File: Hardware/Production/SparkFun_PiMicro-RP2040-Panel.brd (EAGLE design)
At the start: 132.1 x 140.2 mm, 1551 parts, among them J1 Qwiic, J12 USB Female Type C Connector, J13 Qwiic, J16 USB Female Type C Connector, J17 Qwiic, J2 Qwiic, J20 USB Female Type C Connector, J21 Qwiic, J24 USB Female Type C Connector, J25 Qwiic, J28 USB Female Type C Connector, J29 Qwiic, J32 USB Female Type C Connector, J33 Qwiic, J36 USB Female Type C Connector, J37 Qwiic, J40 USB Female Type C Connector, J41 Qwiic, J44 USB Female Type C Connector, J45 Qwiic, J48 USB Female Type C Connector, J49 Qwiic, J5 USB Female Type C Connector, J52 USB Female Type C Connector, J53 Qwiic, J56 USB Female Type C Connector, J57 Qwiic, J60 USB Female Type C Connector, J8 USB Female Type C Connector, J9 Qwiic, U1 3.3V, U10 RP2040, U11 W25QXX128MBIT, U12 WS2812-2020, U13 3.3V, U14 RP2040, U15 W25QXX128MBIT, U16 WS2812-2020, U17 3.3V, U18 RP2040, U19 W25QXX128MBIT, U2 RP2040, U20 WS2812-2020, U21 3.3V, U22 RP2040, U23 W25QXX128MBIT, U24 WS2812-2020, U25 3.3V, U26 RP2040, U27 W25QXX128MBIT, U28 WS2812-2020, U29 3.3V, U3 WS2812-2020, U30 RP2040, U31 W25QXX128MBIT, U32 WS2812-2020, U33 3.3V, U34 RP2040, U35 W25QXX128MBIT, U36 WS2812-2020, U37 3.3V, U38 RP2040, U39 W25QXX128MBIT, U4 W25QXX128MBIT, U40 WS2812-2020, U41 3.3V, U42 RP2040, U43 W25QXX128MBIT, U44 WS2812-2020, U45 3.3V, U46 RP2040, U47 W25QXX128MBIT, U48 WS2812-2020, U49 3.3V, U5 3.3V, U50 RP2040, U51 W25QXX128MBIT, U52 WS2812-2020, U53 3.3V, U54 RP2040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

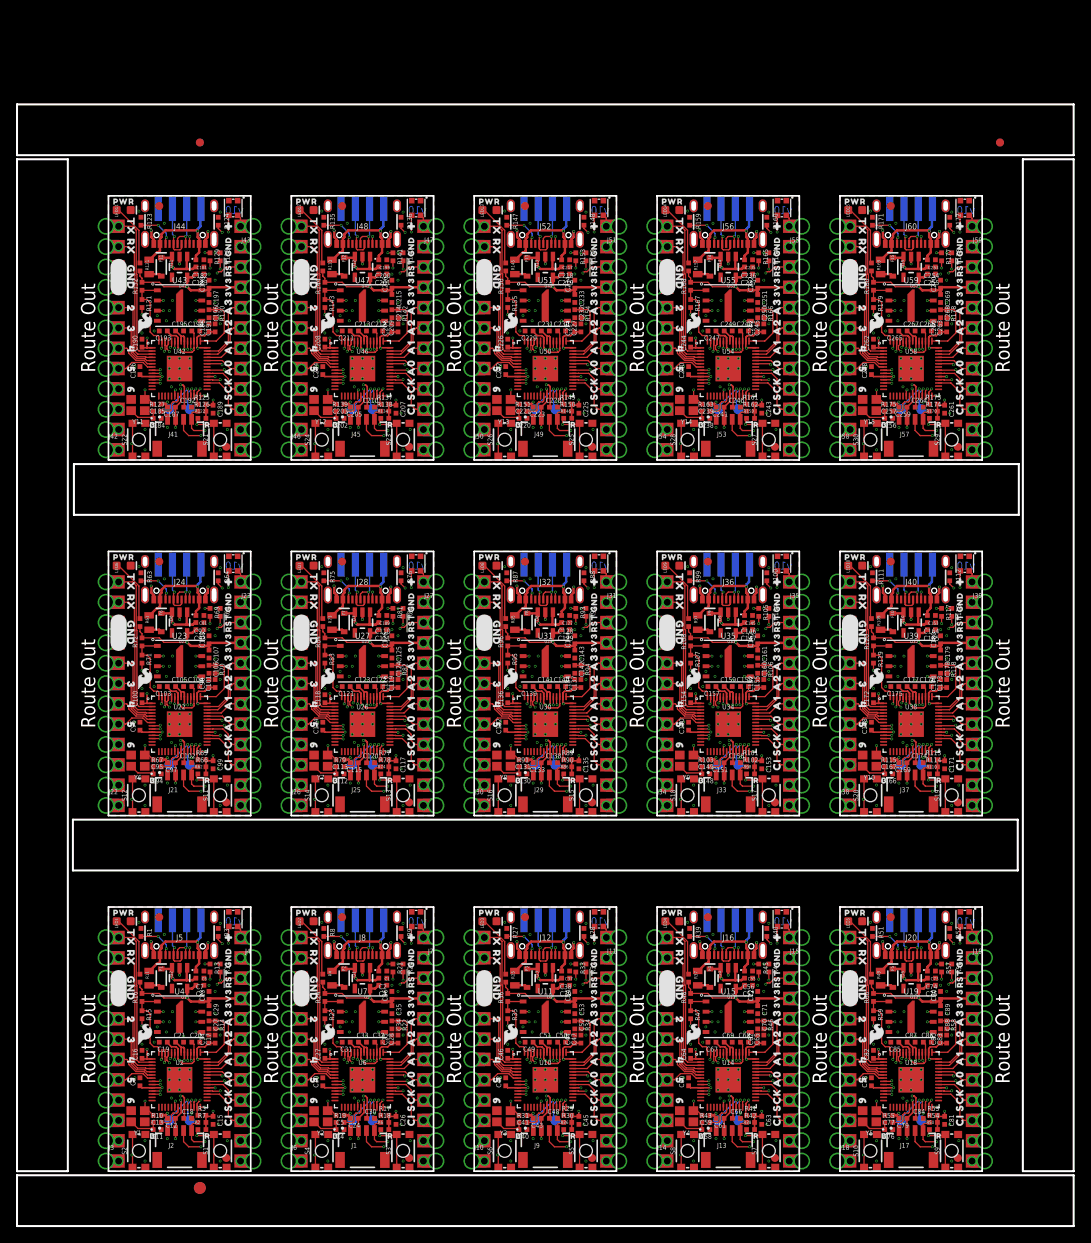
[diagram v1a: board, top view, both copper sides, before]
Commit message: Add DO TP for WS2812
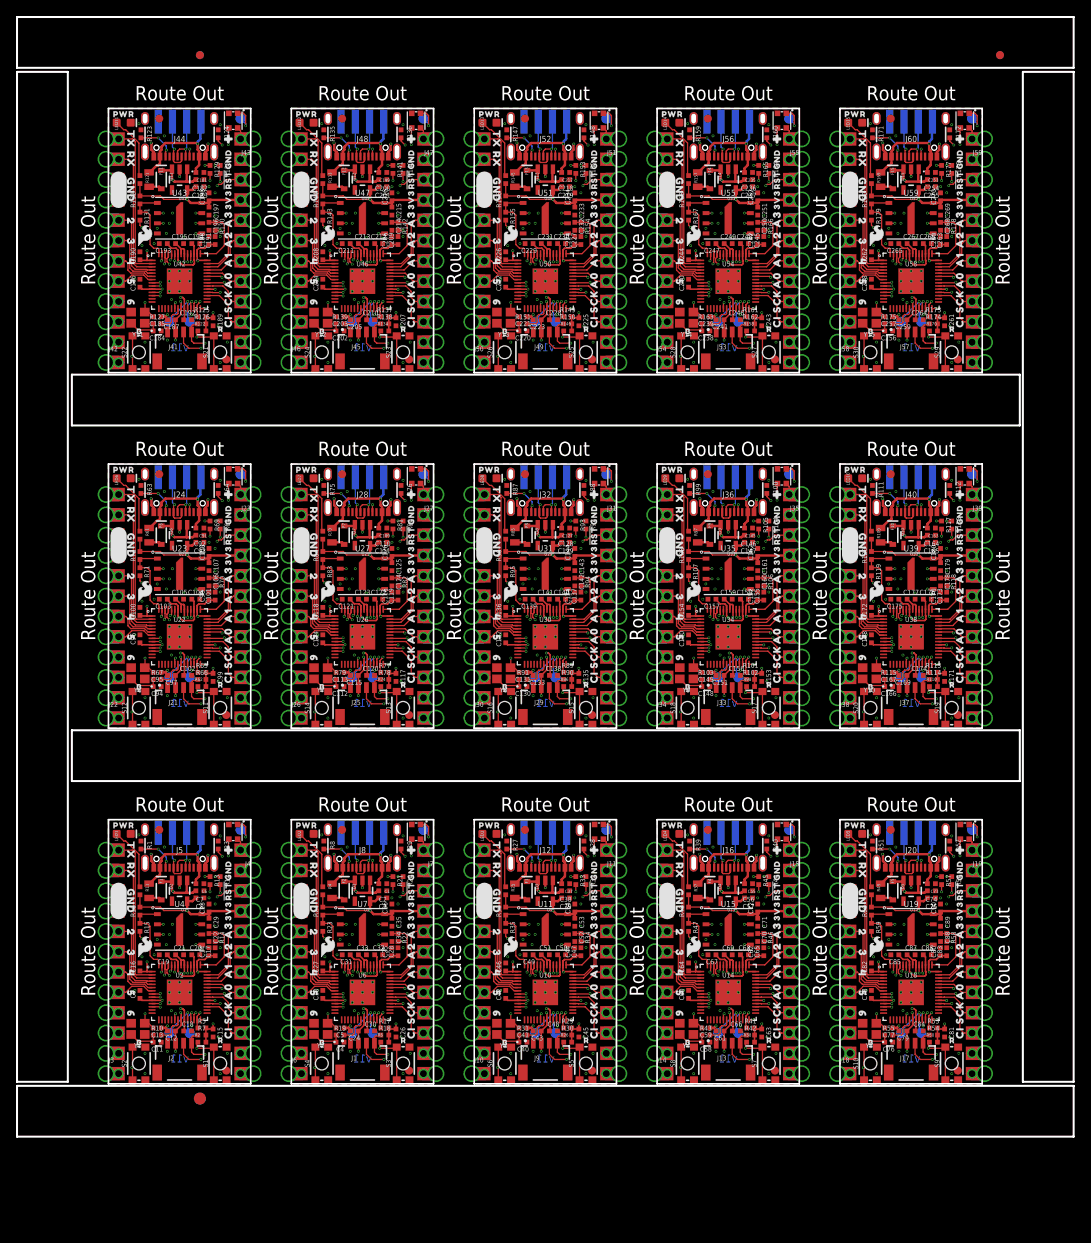
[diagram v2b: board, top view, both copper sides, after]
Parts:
- added TP31, TP32, TP33, TP34, TP35, TP36, TP37, TP38, TP39, TP40, TP41, TP42, TP43, TP44, TP45: (no value), SparkFun-Connectors:PAD.03X.05
- added U$766, U$790: (no value), output:31
- added U$767, U$791: (no value), output:42
- added U$768, U$792: (no value), output:53
- added U$769, U$793: (no value), output:64
- added U$770: (no value), output:#RST#1
- added U$771: (no value), output:3V30
- added U$772: (no value), output:PWR0
- added U$773, U$788, U$801: (no value), output:GND2
- added U$774, U$787: (no value), output:RX1
- added U$775, U$786: (no value), output:TX0
- added U$776: (no value), output:GND_0
- added U$777: (no value), output:70
- added U$778: (no value), output:81
- added U$779: (no value), output:92
- added U$780: (no value), output:CI4
- added U$781: (no value), output:SCK3
- added U$782: (no value), output:A00
- added U$783: (no value), output:A10
- added U$784: (no value), output:A21
- added U$785: (no value), output:A32
- added U$789: (no value), output:20
- added U$794: (no value), output:D#1
- added U$795: (no value), output:D#2
- added U$796: (no value), output:G0
- added U$797: (no value), output:V3
- added U$798: (no value), output:210
- added U$799: (no value), output:#RST#0
- added U$800: (no value), output:3V3_0
- added U$802: (no value), output:RAW0
- added U$803: (no value), output:B0
- added U$804: (no value), output:R0
- added U$805: (no value), output:#0
- added U$806: (no value), output:PRO_MICRO0
- added U$807: (no value), output:RP20401
- added U$808: (no value), output:C0
- added U$809: (no value), output:D1
- added U$810: (no value), output:DO0
- R106, R118, R130, R14, R142, R154, R166, R178, R22, R34, R46, R58, R70, R82, R94: value 200OHM-0402T-1/16W-1% -> 200
- U$100: device output:B0 -> output:RAW0
- U$101: device output:R0 -> output:B0
- U$102: device output:#0 -> output:R0
- U$103: value OSHW-LOGOMINI -> (none); device SparkFun-Aesthetics:OSHW-LOGO-MINI -> output:#0
- U$104, U$536: device output:A00 -> output:PRO_MICRO0
- U$105, U$537: device output:A10 -> output:RP20401
- U$106, U$538: device output:A21 -> output:C0
- U$107, U$539: device output:A32 -> output:D1
- U$108, U$432: device output:CI4 -> output:DO0
- U$109: value (none) -> OSHW-LOGOMINI; device output:CO5 -> SparkFun-Aesthetics:OSHW-LOGO-MINI
- U$110, U$620: device output:SCK3 -> output:A00
- U$111, U$135, U$543, U$621: device output:20 -> output:A10
- U$112, U$136, U$544, U$622: device output:31 -> output:A21
- U$113, U$137, U$545, U$623: device output:42 -> output:A32
- U$114, U$240, U$546, U$726: device output:53 -> output:CI4
- U$115, U$547: device output:64 -> output:CO5
- U$116: device output:#RST#1 -> output:SCK3
- U$117, U$627: device output:3V30 -> output:20
- U$118, U$628: device output:PWR0 -> output:31
- U$119, U$389, U$629: device output:GND2 -> output:42
- U$120, U$630: device output:RX1 -> output:53
- U$121, U$631: device output:TX0 -> output:64
- U$122: device output:GND_0 -> output:#RST#1
- U$123: device output:70 -> output:3V30
- U$124: device output:81 -> output:PWR0
- U$125: device output:92 -> output:GND2
- U$126, U$720: device output:CI4 -> output:RX1
- U$127: device output:SCK3 -> output:TX0
- U$128, U$614: device output:A00 -> output:GND_0
- U$129, U$615: device output:A10 -> output:70
- U$130, U$616: device output:A21 -> output:81
- U$131, U$617: device output:A32 -> output:92
- U$132, U$438: device output:TX0 -> output:CI4
- U$133: device output:RX1 -> output:SCK3
- U$134, U$272, U$542: device output:GND2 -> output:A00
- U$138, U$624: device output:53 -> output:TX0
- U$139, U$625: device output:64 -> output:RX1
- U$140, U$395: device output:D#1 -> output:GND2
- U$141, U$549: device output:D#2 -> output:20
- U$142, U$550: device output:G0 -> output:31
- U$143, U$551: device output:V3 -> output:42
- U$144, U$552: device output:210 -> output:53
- U$145, U$553: device output:#RST#0 -> output:64
- U$146: device output:3V3_0 -> output:D#1
- U$147: device output:GND2 -> output:D#2
- U$148: device output:PIMICRO0 -> output:G0
- U$149: device output:RP20400 -> output:V3
- U$150: device output:RAW0 -> output:210
- U$151: device output:B0 -> output:#RST#0
- U$152: device output:R0 -> output:3V3_0
- U$153: device output:#0 -> output:GND2
- U$154: value OSHW-LOGOMINI -> (none); device SparkFun-Aesthetics:OSHW-LOGO-MINI -> output:RAW0
- U$155, U$587: device output:A00 -> output:B0
- U$156, U$588: device output:A10 -> output:R0
- U$157, U$589: device output:A21 -> output:#0
- U$158, U$590: device output:A32 -> output:PRO_MICRO0
- U$159, U$483: device output:CI4 -> output:RP20401
- U$160: device output:CO5 -> output:C0
- U$161: device output:SCK3 -> output:D1
- U$162, U$594: device output:20 -> output:DO0
- U$163, U$595: value (none) -> OSHW-LOGOMINI; device output:31 -> SparkFun-Aesthetics:OSHW-LOGO-MINI
- U$164, U$188, U$596, U$674: device output:42 -> output:A00
- U$165, U$189, U$597, U$675: device output:53 -> output:A10
- U$166, U$190, U$598, U$676: device output:64 -> output:A21
- U$167, U$677: device output:#RST#1 -> output:A32
- U$168: device output:3V30 -> output:CI4
- U$169: device output:PWR0 -> output:CO5
- U$170, U$440: device output:GND2 -> output:SCK3
- U$171, U$681: device output:RX1 -> output:20
- U$172, U$682: device output:TX0 -> output:31
- U$173, U$683: device output:GND_0 -> output:42
- U$174, U$684: device output:70 -> output:53
- U$175, U$685: device output:81 -> output:64
- U$176: device output:92 -> output:#RST#1
- U$177: device output:CI4 -> output:3V30
- U$178: device output:SCK3 -> output:PWR0
- U$179, U$410, U$665: device output:A00 -> output:GND2
- U$18: device output:PIMICRO0 -> output:C0
- U$180, U$666: device output:A10 -> output:RX1
- U$181, U$667: device output:A21 -> output:TX0
- U$182, U$668: device output:A32 -> output:GND_0
- U$183: device output:TX0 -> output:70
- U$184: device output:RX1 -> output:81
- U$185: device output:GND2 -> output:92
- U$186, U$46, U$492, U$672: device output:20 -> output:CI4
- U$187, U$673: device output:31 -> output:SCK3
- U$191, U$599: device output:D#1 -> output:A32
- U$192: device output:D#2 -> output:TX0
- U$193: device output:G0 -> output:RX1
- U$194, U$449: device output:V3 -> output:GND2
- U$195, U$603: device output:210 -> output:20
- U$196, U$604: device output:#RST#0 -> output:31
- U$197, U$605: device output:3V3_0 -> output:42
- U$198, U$606: device output:GND2 -> output:53
- U$199, U$607: device output:PIMICRO0 -> output:64
- U$200: device output:RP20400 -> output:D#1
- U$201: device output:RAW0 -> output:D#2
- U$202: device output:B0 -> output:G0
- U$203: device output:R0 -> output:V3
- U$204: device output:#0 -> output:210
- U$205: value OSHW-LOGOMINI -> (none); device SparkFun-Aesthetics:OSHW-LOGO-MINI -> output:#RST#0
- U$206, U$638: device output:A00 -> output:3V3_0
- U$207, U$639: device output:A10 -> output:GND2
- U$208, U$640: device output:A21 -> output:RAW0
- U$209, U$641: device output:A32 -> output:B0
- U$210, U$534: device output:CI4 -> output:R0
- U$211: device output:CO5 -> output:#0
- U$212: device output:SCK3 -> output:PRO_MICRO0
- U$213, U$645: device output:20 -> output:RP20401
- U$214, U$646: device output:31 -> output:C0
- U$215, U$647: device output:42 -> output:D1
- U$216, U$648: device output:53 -> output:DO0
- U$217, U$649: value (none) -> OSHW-LOGOMINI; device output:64 -> SparkFun-Aesthetics:OSHW-LOGO-MINI
- U$218, U$728: device output:#RST#1 -> output:A00
- U$219, U$729: device output:3V30 -> output:A10
- U$220, U$730: device output:PWR0 -> output:A21
- U$221, U$491, U$731, U$83: device output:GND2 -> output:A32
- U$222: device output:RX1 -> output:CI4
- U$223: device output:TX0 -> output:CO5
- U$224: device output:GND_0 -> output:SCK3
- U$225, U$735: device output:70 -> output:20
- U$226, U$736: device output:81 -> output:31
- U$227, U$737: device output:92 -> output:42
- U$228, U$414, U$738: device output:CI4 -> output:53
- U$229, U$739: device output:SCK3 -> output:64
- U$230, U$716: device output:A00 -> output:#RST#1
- U$231, U$717: device output:A10 -> output:3V30
- U$232, U$718: device output:A21 -> output:PWR0
- U$233, U$464, U$719: device output:A32 -> output:GND2
- U$234, U$733: device output:TX0 -> output:RX1
- U$235, U$732: device output:RX1 -> output:TX0
- U$236: device output:GND2 -> output:GND_0
- U$237, U$723: device output:20 -> output:70
- U$238, U$724: device output:31 -> output:81
- U$239, U$725: device output:42 -> output:92
- U$241, U$727: device output:64 -> output:SCK3
- U$242, U$650: device output:D#1 -> output:A00
- U$243, U$651: device output:D#2 -> output:A10
- U$244, U$652: device output:G0 -> output:A21
- U$245, U$653: device output:V3 -> output:A32
- U$246: device output:210 -> output:TX0
- U$247: device output:#RST#0 -> output:RX1
- U$248, U$503: device output:3V3_0 -> output:GND2
- U$249, U$657: device output:GND2 -> output:20
- U$250, U$658: device output:PIMICRO0 -> output:31
- U$251, U$659: device output:RP20400 -> output:42
- U$252, U$660: device output:RAW0 -> output:53
- U$253, U$661: device output:B0 -> output:64
- U$254: device output:R0 -> output:D#1
- U$255: device output:#0 -> output:D#2
- U$256: value OSHW-LOGOMINI -> (none); device SparkFun-Aesthetics:OSHW-LOGO-MINI -> output:G0
- U$257, U$689: device output:A00 -> output:V3
- U$258, U$690: device output:A10 -> output:210
- U$259, U$691: device output:A21 -> output:#RST#0
- U$260, U$692: device output:A32 -> output:3V3_0
- U$261, U$585: device output:CI4 -> output:GND2
- U$262: device output:CO5 -> output:RAW0
- U$263: device output:SCK3 -> output:B0
- U$264, U$696: device output:20 -> output:R0
- U$265, U$697: device output:31 -> output:#0
- U$266, U$698: device output:42 -> output:PRO_MICRO0
- U$267, U$699: device output:53 -> output:RP20401
- U$268, U$700: device output:64 -> output:C0
- U$269: device output:#RST#1 -> output:D1
- U$270: device output:3V30 -> output:DO0
- U$271: value (none) -> OSHW-LOGOMINI; device output:PWR0 -> SparkFun-Aesthetics:OSHW-LOGO-MINI
- U$273: device output:RX1 -> output:A10
- U$274: device output:TX0 -> output:A21
- U$275: device output:GND_0 -> output:A32
- U$276: device output:70 -> output:CI4
- U$277: device output:81 -> output:CO5
- U$278: device output:92 -> output:SCK3
- U$279, U$465: device output:CI4 -> output:20
- U$280: device output:SCK3 -> output:31
- U$281, U$359: device output:A00 -> output:42
- U$282, U$360: device output:A10 -> output:53
- U$283, U$361: device output:A21 -> output:64
- U$284: device output:A32 -> output:#RST#1
- U$285: device output:TX0 -> output:3V30
- U$286: device output:RX1 -> output:PWR0
- U$288: device output:20 -> output:RX1
- U$289: device output:31 -> output:TX0
- U$290: device output:42 -> output:GND_0
- U$291: device output:53 -> output:70
- U$292: device output:64 -> output:81
- U$293: device output:D#1 -> output:92
- U$294, U$600: device output:D#2 -> output:CI4
- U$295: device output:G0 -> output:SCK3
- U$296, U$704: device output:V3 -> output:A00
- U$297, U$705: device output:210 -> output:A10
- U$298, U$706: device output:#RST#0 -> output:A21
- U$299, U$707: device output:3V3_0 -> output:A32
- U$300: device output:GND2 -> output:TX0
- U$301: device output:PIMICRO0 -> output:RX1
- U$302, U$557: device output:RP20400 -> output:GND2
- U$303, U$711: device output:RAW0 -> output:20
- U$304, U$712: device output:B0 -> output:31
- U$305, U$713: device output:R0 -> output:42
- U$306, U$714: device output:#0 -> output:53
- U$307, U$715: value OSHW-LOGOMINI -> (none); device SparkFun-Aesthetics:OSHW-LOGO-MINI -> output:64
- U$308, U$740: device output:A00 -> output:D#1
- U$309, U$741: device output:A10 -> output:D#2
- U$310, U$742: device output:A21 -> output:G0
- U$311, U$743: device output:A32 -> output:V3
- U$312, U$636: device output:CI4 -> output:210
- U$313: device output:CO5 -> output:#RST#0
- U$314: device output:SCK3 -> output:3V3_0
- U$315, U$747: device output:20 -> output:GND2
- U$316, U$748: device output:31 -> output:RAW0
- U$317, U$749: device output:42 -> output:B0
- U$318, U$750: device output:53 -> output:R0
- U$319, U$751: device output:64 -> output:#0
- U$320: device output:#RST#1 -> output:PRO_MICRO0
- U$321: device output:3V30 -> output:RP20401
- U$322: device output:PWR0 -> output:C0
- U$323, U$593: device output:GND2 -> output:D1
- U$324: device output:RX1 -> output:DO0
- U$325: value (none) -> OSHW-LOGOMINI; device output:TX0 -> SparkFun-Aesthetics:OSHW-LOGO-MINI
- U$326: device output:GND_0 -> output:A00
- U$327: device output:70 -> output:A10
- U$328: device output:81 -> output:A21
- U$329: device output:92 -> output:A32
- U$331: device output:SCK3 -> output:CO5
- U$332: device output:A00 -> output:SCK3
- U$333, U$411: device output:A10 -> output:20
- U$334, U$412: device output:A21 -> output:31
- U$335, U$413: device output:A32 -> output:42
- U$336: device output:TX0 -> output:53
- U$337: device output:RX1 -> output:64
- U$338, U$59: device output:GND2 -> output:#RST#1
- U$339: device output:20 -> output:3V30
- U$340: device output:31 -> output:PWR0
- U$341, U$572, U$86: device output:42 -> output:GND2
- U$342: device output:53 -> output:RX1
- U$343: device output:64 -> output:TX0
- U$344: device output:D#1 -> output:GND_0
- U$345: device output:D#2 -> output:70
- U$346: device output:G0 -> output:81
- U$347: device output:V3 -> output:92
- U$348, U$654: device output:210 -> output:CI4
- U$349: device output:#RST#0 -> output:SCK3
- U$35: device output:RP20400 -> output:D1
- U$350, U$758: device output:3V3_0 -> output:A00
- U$351, U$759: device output:GND2 -> output:A10
- U$352, U$760: device output:PIMICRO0 -> output:A21
- U$353, U$761: device output:RP20400 -> output:A32
- U$354: device output:RAW0 -> output:TX0
- U$355: device output:B0 -> output:RX1
- U$356, U$611: device output:R0 -> output:GND2
- U$357, U$765: device output:#0 -> output:20
- U$358: value OSHW-LOGOMINI -> (none); device SparkFun-Aesthetics:OSHW-LOGO-MINI -> output:31
- U$362: device output:A32 -> output:D#1
- U$363, U$687: device output:CI4 -> output:D#2
- U$364: device output:CO5 -> output:G0
- U$365: device output:SCK3 -> output:V3
- U$366: device output:20 -> output:210
- U$367: device output:31 -> output:#RST#0
- U$368: device output:42 -> output:3V3_0
- U$369: device output:53 -> output:GND2
- U$370: device output:64 -> output:RAW0
- U$371: device output:#RST#1 -> output:B0
- U$372: device output:3V30 -> output:R0
- U$373: device output:PWR0 -> output:#0
- U$374, U$644: device output:GND2 -> output:PRO_MICRO0
- U$375: device output:RX1 -> output:RP20401
- U$376: device output:TX0 -> output:C0
- U$377: device output:GND_0 -> output:D1
- U$378: device output:70 -> output:DO0
- U$379: value (none) -> OSHW-LOGOMINI; device output:81 -> SparkFun-Aesthetics:OSHW-LOGO-MINI
- U$38: device output:A00 -> output:RP20401
- U$380: device output:92 -> output:A00
- U$381, U$43, U$567: device output:CI4 -> output:A10
- U$382: device output:SCK3 -> output:A21
- U$383, U$461: device output:A00 -> output:A32
- U$384, U$564, U$78: device output:A10 -> output:CI4
- U$385: device output:A21 -> output:CO5
- U$386: device output:A32 -> output:SCK3
- U$387: device output:TX0 -> output:20
- U$388: device output:RX1 -> output:31
- U$390, U$468: device output:20 -> output:53
- U$391, U$469: device output:31 -> output:64
- U$392: device output:42 -> output:#RST#1
- U$393: device output:53 -> output:3V30
- U$394: device output:64 -> output:PWR0
- U$396: device output:D#2 -> output:RX1
- U$397: device output:G0 -> output:TX0
- U$398: device output:V3 -> output:GND_0
- U$399: device output:210 -> output:70
- U$4: value OSHW-LOGOMINI -> (none); device SparkFun-Aesthetics:OSHW-LOGO-MINI -> output:PRO_MICRO0
- U$40, U$486: device output:A10 -> output:DO0
- U$400: device output:#RST#0 -> output:81
- U$401: device output:3V3_0 -> output:92
- U$402, U$708: device output:GND2 -> output:CI4
- U$403: device output:PIMICRO0 -> output:SCK3
- U$404: device output:RP20400 -> output:A00
- U$405: device output:RAW0 -> output:A10
- U$406: device output:B0 -> output:A21
- U$407: device output:R0 -> output:A32
- U$408: device output:#0 -> output:TX0
- U$409: value OSHW-LOGOMINI -> (none); device SparkFun-Aesthetics:OSHW-LOGO-MINI -> output:RX1
- U$41, U$487: value (none) -> OSHW-LOGOMINI; device output:A21 -> SparkFun-Aesthetics:OSHW-LOGO-MINI
- U$415: device output:CO5 -> output:64
- U$416: device output:SCK3 -> output:D#1
- U$417: device output:20 -> output:D#2
- U$418: device output:31 -> output:G0
- U$419: device output:42 -> output:V3
- U$42, U$488, U$566, U$80: device output:A32 -> output:A00
- U$420: device output:53 -> output:210
- U$421: device output:64 -> output:#RST#0
- U$422: device output:#RST#1 -> output:3V3_0
- U$423: device output:3V30 -> output:GND2
- U$424: device output:PWR0 -> output:RAW0
- U$425, U$695: device output:GND2 -> output:B0
- U$426: device output:RX1 -> output:R0
- U$427: device output:TX0 -> output:#0
- U$428: device output:GND_0 -> output:PRO_MICRO0
- U$429: device output:70 -> output:RP20401
- U$430: device output:81 -> output:C0
- U$431: device output:92 -> output:D1
- U$433: value (none) -> OSHW-LOGOMINI; device output:SCK3 -> SparkFun-Aesthetics:OSHW-LOGO-MINI
- U$439: device output:RX1 -> output:CO5
- U$44, U$568: device output:CO5 -> output:A21
- U$446: device output:D#1 -> output:#RST#1
- U$447: device output:D#2 -> output:3V30
- U$448: device output:G0 -> output:PWR0
- U$45, U$569: device output:SCK3 -> output:A32
- U$450: device output:210 -> output:RX1
- U$451: device output:#RST#0 -> output:TX0
- U$452: device output:3V3_0 -> output:GND_0
- U$453: device output:GND2 -> output:70
- U$454: device output:PIMICRO0 -> output:81
- U$455: device output:RP20400 -> output:92
- U$456, U$762: device output:RAW0 -> output:CI4
- U$457: device output:B0 -> output:SCK3
- U$458: device output:R0 -> output:A00
- U$459: device output:#0 -> output:A10
- U$460: value OSHW-LOGOMINI -> (none); device SparkFun-Aesthetics:OSHW-LOGO-MINI -> output:A21
- U$462: device output:A10 -> output:TX0
- U$463: device output:A21 -> output:RX1
- U$466: device output:CO5 -> output:31
- U$467: device output:SCK3 -> output:42
- U$47, U$493: device output:31 -> output:CO5
- U$470: device output:42 -> output:D#1
- U$471: device output:53 -> output:D#2
- U$472: device output:64 -> output:G0
- U$473: device output:#RST#1 -> output:V3
- U$474: device output:3V30 -> output:210
- U$475: device output:PWR0 -> output:#RST#0
- U$476, U$746: device output:GND2 -> output:3V3_0
- U$477: device output:RX1 -> output:GND2
- U$478: device output:TX0 -> output:RAW0
- U$479: device output:GND_0 -> output:B0
- U$48, U$494: device output:42 -> output:SCK3
- U$480: device output:70 -> output:R0
- U$481: device output:81 -> output:#0
- U$482: device output:92 -> output:PRO_MICRO0
- U$484: device output:SCK3 -> output:C0
- U$485: device output:A00 -> output:D1
- U$489, U$81: device output:TX0 -> output:A10
- U$49, U$495, U$573, U$87: device output:53 -> output:20
- U$490, U$82: device output:RX1 -> output:A21
- U$496, U$50, U$574, U$88: device output:64 -> output:31
- U$497, U$89: device output:D#1 -> output:42
- U$498, U$90: device output:D#2 -> output:53
- U$499, U$91: device output:G0 -> output:64
- U$500: device output:V3 -> output:#RST#1
- U$501: device output:210 -> output:3V30
- U$502: device output:#RST#0 -> output:PWR0
- U$504: device output:GND2 -> output:RX1
- U$505: device output:PIMICRO0 -> output:TX0
- U$506: device output:RP20400 -> output:GND_0
- U$507: device output:RAW0 -> output:70
- U$508: device output:B0 -> output:81
- U$509: device output:R0 -> output:92
- U$51, U$575: device output:#RST#1 -> output:42
- U$510: device output:#0 -> output:CI4
- U$511: value OSHW-LOGOMINI -> (none); device SparkFun-Aesthetics:OSHW-LOGO-MINI -> output:SCK3
- U$516: device output:CI4 -> output:TX0
- U$517: device output:CO5 -> output:RX1
- U$518: device output:SCK3 -> output:GND2
- U$52, U$576: device output:3V30 -> output:53
- U$524: device output:#RST#1 -> output:D#1
- U$525: device output:3V30 -> output:D#2
- U$526: device output:PWR0 -> output:G0
- U$527: device output:GND2 -> output:V3
- U$528: device output:RX1 -> output:210
- U$529: device output:TX0 -> output:#RST#0
- U$530: device output:GND_0 -> output:3V3_0
- U$531: device output:70 -> output:GND2
- U$532: device output:81 -> output:RAW0
- U$533: device output:92 -> output:B0
- U$535: device output:SCK3 -> output:#0
- U$540: device output:TX0 -> output:DO0
- U$541: value (none) -> OSHW-LOGOMINI; device output:RX1 -> SparkFun-Aesthetics:OSHW-LOGO-MINI
- U$548: device output:D#1 -> output:SCK3
- U$554: device output:3V3_0 -> output:#RST#1
- U$555: device output:GND2 -> output:3V30
- U$556: device output:PIMICRO0 -> output:PWR0
- U$558: device output:RAW0 -> output:RX1
- U$559: device output:B0 -> output:TX0
- U$560: device output:R0 -> output:GND_0
- U$561: device output:#0 -> output:70
- U$562: value OSHW-LOGOMINI -> (none); device SparkFun-Aesthetics:OSHW-LOGO-MINI -> output:81
- U$563, U$77: device output:A00 -> output:92
- U$565, U$79: device output:A21 -> output:SCK3
- U$570, U$84: device output:20 -> output:TX0
- U$571, U$85: device output:31 -> output:RX1
- U$577, U$58: device output:PWR0 -> output:64
- U$578: device output:GND2 -> output:D#1
- U$579: device output:RX1 -> output:D#2
- U$580: device output:TX0 -> output:G0
- U$581: device output:GND_0 -> output:V3
- U$582: device output:70 -> output:210
- U$583: device output:81 -> output:#RST#0
- U$584: device output:92 -> output:3V3_0
- U$586: device output:SCK3 -> output:RAW0
- U$591: device output:TX0 -> output:RP20401
- U$592: device output:RX1 -> output:C0
- U$60: device output:RX1 -> output:3V30
- U$601: device output:G0 -> output:CO5
- U$602: device output:V3 -> output:SCK3
- U$608: device output:RP20400 -> output:#RST#1
- U$609: device output:RAW0 -> output:3V30
- U$61: device output:TX0 -> output:PWR0
- U$610: device output:B0 -> output:PWR0
- U$612: device output:#0 -> output:RX1
- U$613: value OSHW-LOGOMINI -> (none); device SparkFun-Aesthetics:OSHW-LOGO-MINI -> output:TX0
- U$619: device output:CO5 -> output:SCK3
- U$62, U$734: device output:GND_0 -> output:GND2
- U$626: device output:#RST#1 -> output:GND2
- U$63: device output:70 -> output:RX1
- U$632: device output:GND_0 -> output:D#1
- U$633: device output:70 -> output:D#2
- U$634: device output:81 -> output:G0
- U$635: device output:92 -> output:V3
- U$637: device output:SCK3 -> output:#RST#0
- U$642: device output:TX0 -> output:R0
- U$643: device output:RX1 -> output:#0
- U$65: device output:81 -> output:TX0
- U$655: device output:#RST#0 -> output:CO5
- U$656: device output:3V3_0 -> output:SCK3
- U$662: device output:R0 -> output:#RST#1
- U$663: device output:#0 -> output:3V30
- U$664: value OSHW-LOGOMINI -> (none); device SparkFun-Aesthetics:OSHW-LOGO-MINI -> output:PWR0
- U$669, U$71: device output:CI4 -> output:70
- U$670: device output:CO5 -> output:81
- U$671: device output:SCK3 -> output:92
- U$678: device output:3V30 -> output:TX0
- U$679: device output:PWR0 -> output:RX1
- U$686: device output:92 -> output:D#1
- U$688: device output:SCK3 -> output:G0
- U$693: device output:TX0 -> output:GND2
- U$694: device output:RX1 -> output:RAW0
- U$70: device output:92 -> output:GND_0
- U$701: device output:D#1 -> output:D1
- U$702: device output:D#2 -> output:DO0
- U$703: value (none) -> OSHW-LOGOMINI; device output:G0 -> SparkFun-Aesthetics:OSHW-LOGO-MINI
- U$709: device output:PIMICRO0 -> output:CO5
- U$710: device output:RP20400 -> output:SCK3
- U$72: device output:SCK3 -> output:81
- U$721: device output:CO5 -> output:TX0
- U$722: device output:SCK3 -> output:GND_0
- U$744: device output:TX0 -> output:210
- U$745: device output:RX1 -> output:#RST#0
- U$752: device output:D#1 -> output:PRO_MICRO0
- U$753: device output:D#2 -> output:RP20401
- U$754: device output:G0 -> output:C0
- U$755: device output:V3 -> output:D1
- U$756: device output:210 -> output:DO0
- U$757: value (none) -> OSHW-LOGOMINI; device output:#RST#0 -> SparkFun-Aesthetics:OSHW-LOGO-MINI
- U$763: device output:B0 -> output:CO5
- U$764: device output:R0 -> output:SCK3
- U$92: device output:V3 -> output:D#1
- U$93: device output:210 -> output:D#2
- U$94: device output:#RST#0 -> output:G0
- U$95: device output:3V3_0 -> output:V3
- U$96: device output:GND2 -> output:210
- U$97: device output:PIMICRO0 -> output:#RST#0
- U$98: device output:RP20400 -> output:3V3_0
- U$99: device output:RAW0 -> output:GND2
- moved U$528 118.9 mm to (106.0, 45.7), flipped to the bottom, turned to 0 degrees
- moved U$511 117.6 mm to (105.5, 53.3)
- moved U$264 112.9 mm to (105.5, 5.41), turned to 0 degrees
- moved U$529 109.5 mm to (105.3, 68.6), flipped to the bottom, turned to 0 degrees
- moved U$540 107.7 mm to (106.4, 76.1), turned to 270 degrees
- moved U$265 105.8 mm to (106.5, 29.2), turned to 0 degrees
- moved U$267 104.6 mm to (102.9, 14.4), flipped to the bottom
- moved U$531 104.6 mm to (106.4, 71.1), turned to 270 degrees
- moved U$527 103.9 mm to (103.0, 73.4), flipped to the bottom
- moved U$266 103.4 mm to (100.8, 14.5), flipped to the bottom
- moved U$532 103.2 mm to (105.5, 73.7)
- moved U$268 103.1 mm to (98.9, 4.95), flipped to the bottom, turned to 0 degrees
- moved U$526 102.6 mm to (97.7, 73.5), flipped to the bottom, turned to 270 degrees
- moved U$258 102.2 mm to (106.0, 1.27), flipped to the bottom, turned to 0 degrees
- moved U$256 102.1 mm to (97.7, 29.1), turned to 270 degrees
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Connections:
- new net N$1: TP3.P$1, U3.1
- new net N$11: TP9.P$1, U12.1
- new net N$15: TP12.P$1, U16.1
- new net N$19: TP15.P$1, U20.1
- new net N$23: TP18.P$1, U24.1
- new net N$27: TP21.P$1, U28.1
- new net N$31: TP24.P$1, U32.1
- new net N$35: TP27.P$1, U36.1
- new net N$40: TP30.P$1, U40.1
- new net N$44: TP33.P$1, U44.1
- new net N$48: TP36.P$1, U48.1
- new net N$5: TP6.P$1, U8.1
- new net N$52: TP39.P$1, U52.1
- new net N$56: TP42.P$1, U56.1
- new net N$60: TP45.P$1, U60.1
- net SWDCK1: now also TP4.P$1; no longer TP3.P$1
- net SWDCK10: now also TP31.P$1; no longer TP21.P$1
- net SWDCK11: now also TP34.P$1; no longer TP23.P$1
- net SWDCK12: now also TP37.P$1; no longer TP25.P$1
- net SWDCK13: now also TP40.P$1; no longer TP27.P$1
- net SWDCK14: now also TP43.P$1; no longer TP29.P$1
- net SWDCK2: now also TP7.P$1; no longer TP5.P$1
- net SWDCK3: now also TP10.P$1; no longer TP7.P$1
- net SWDCK4: now also TP13.P$1; no longer TP9.P$1
- net SWDCK5: now also TP16.P$1; no longer TP11.P$1
- net SWDCK6: now also TP19.P$1; no longer TP13.P$1
- net SWDCK7: now also TP22.P$1; no longer TP15.P$1
- net SWDCK8: now also TP25.P$1; no longer TP17.P$1
- net SWDCK9: now also TP28.P$1; no longer TP19.P$1
- net SWDIO1: now also TP5.P$1; no longer TP4.P$1
- net SWDIO10: now also TP32.P$1; no longer TP22.P$1
- net SWDIO11: now also TP35.P$1; no longer TP24.P$1
- net SWDIO12: now also TP38.P$1; no longer TP26.P$1
- net SWDIO13: now also TP41.P$1; no longer TP28.P$1
- net SWDIO14: now also TP44.P$1; no longer TP30.P$1
- net SWDIO2: now also TP8.P$1; no longer TP6.P$1
- net SWDIO3: now also TP11.P$1; no longer TP8.P$1
- net SWDIO4: now also TP14.P$1; no longer TP10.P$1
- net SWDIO5: now also TP17.P$1; no longer TP12.P$1
- net SWDIO6: now also TP20.P$1; no longer TP14.P$1
- net SWDIO7: now also TP23.P$1; no longer TP16.P$1
- net SWDIO8: now also TP26.P$1; no longer TP18.P$1
- net SWDIO9: now also TP29.P$1; no longer TP20.P$1
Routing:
- net N$52: track 0.00 -> 3.53 mm, vias 0 -> 1
- net N$48: track 0.00 -> 3.53 mm, vias 0 -> 1
- net N$44: track 0.00 -> 3.53 mm, vias 0 -> 1
- net N$11: track 0.00 -> 3.53 mm, vias 0 -> 1
- net N$5: track 0.00 -> 3.53 mm, vias 0 -> 1
- net N$60: track 0.00 -> 3.53 mm, vias 0 -> 1
- net N$56: track 0.00 -> 3.53 mm, vias 0 -> 1
- net N$1: track 0.00 -> 3.53 mm, vias 0 -> 1
- net N$31: track 0.00 -> 3.53 mm, vias 0 -> 1
- net N$27: track 0.00 -> 3.53 mm, vias 0 -> 1
- net N$23: track 0.00 -> 3.53 mm, vias 0 -> 1
- net N$19: track 0.00 -> 3.53 mm, vias 0 -> 1
- net N$15: track 0.00 -> 3.53 mm, vias 0 -> 1
- net N$40: track 0.00 -> 3.53 mm, vias 0 -> 1
- net N$35: track 0.00 -> 3.53 mm, vias 0 -> 1
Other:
- board size 132.1 x 140.2 mm -> 132.1 x 140 mm
- board text added: "v11"
- board text removed: "v10"
